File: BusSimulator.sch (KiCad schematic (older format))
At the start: 100 parts, among them IC1 CS30CL, IC2 CS30CL, IC3 CS30CL, J1 CONN_3-6318491-6, J2 OSTTA024163, J3 Conn_01x03, J4 Conn_01x03, J5 Conn_01x02, J6 Conn_01x03, Q1 MOSFET_N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

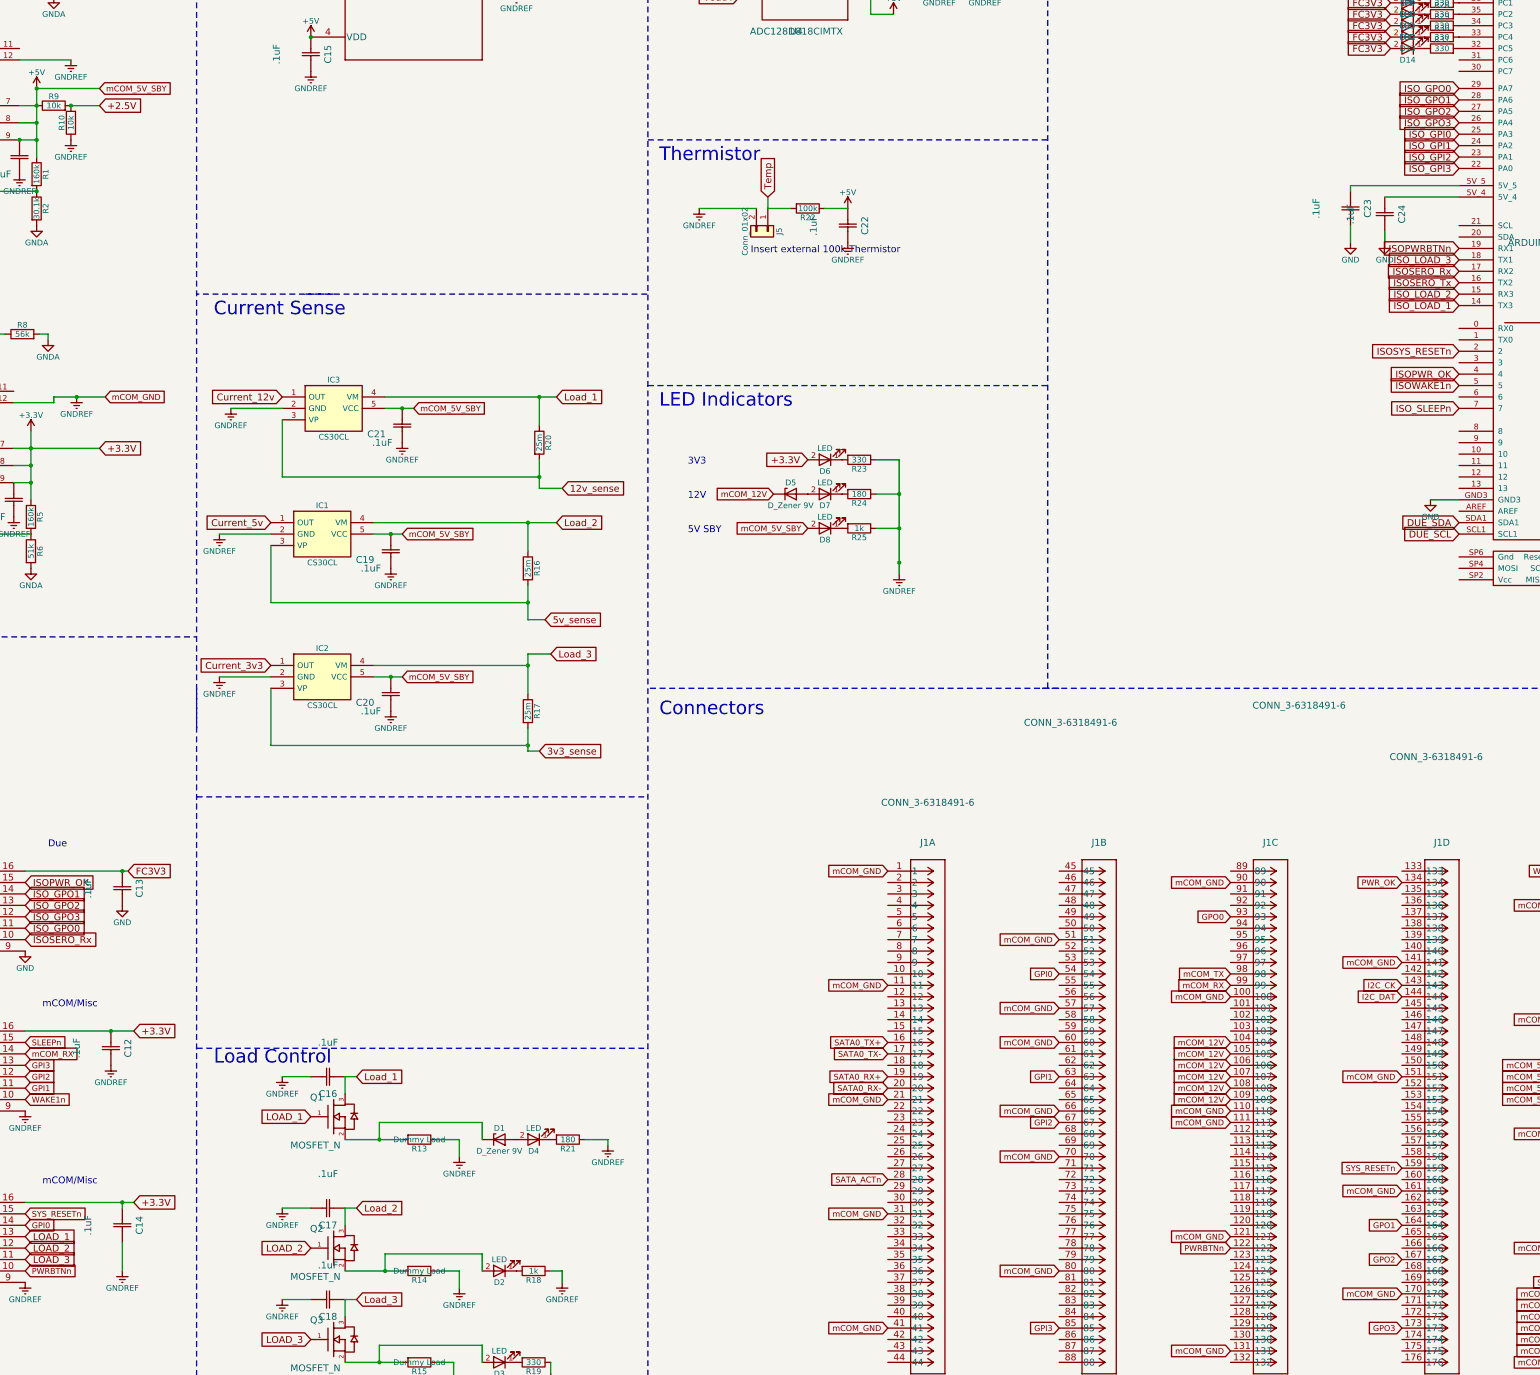
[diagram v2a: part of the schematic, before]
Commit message: Routed mCOM connector and isolators
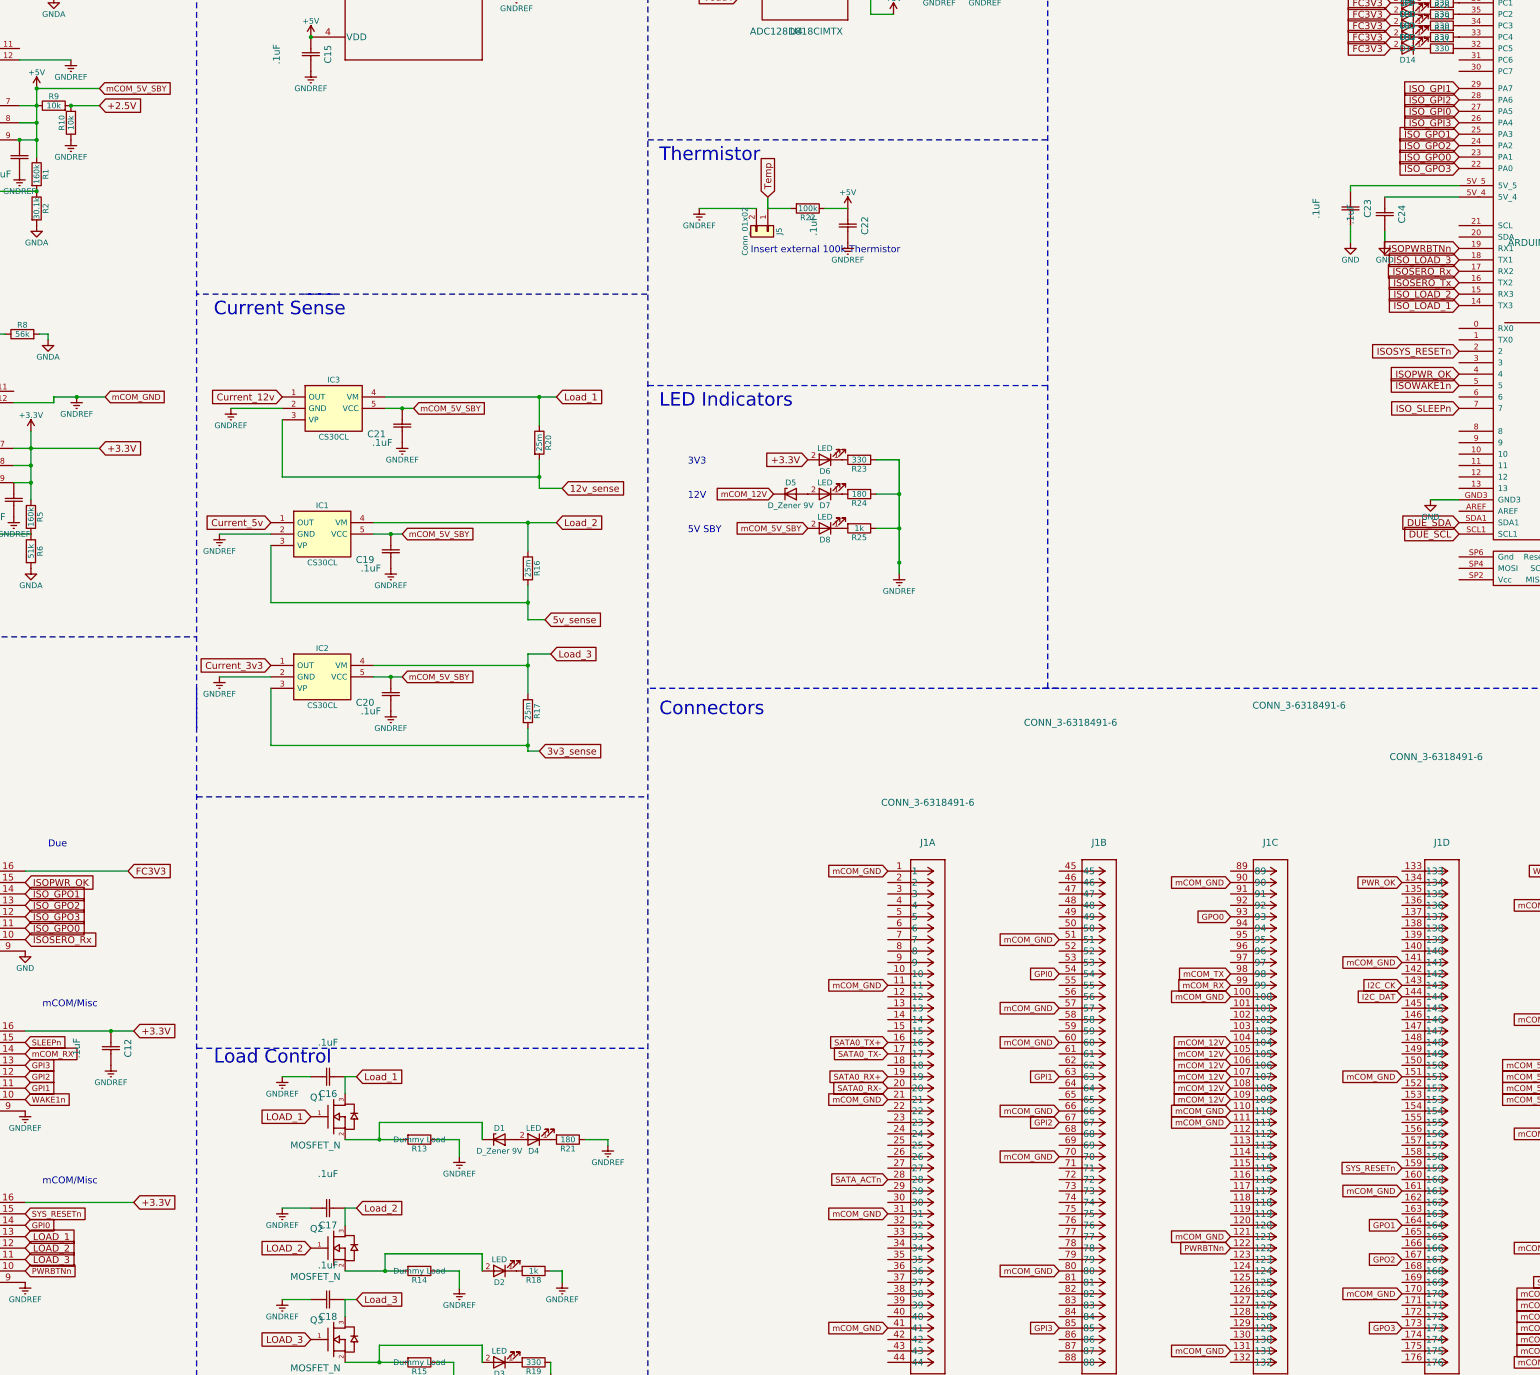
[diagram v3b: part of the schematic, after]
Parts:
- removed C13, C14: .1uF, Capacitors_SMD:C_0603, symbol CAPH
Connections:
- net ISO_GPI0: now also SHIELD1.27 (PA5); no longer SHIELD1.25 (PA3)
- net ISO_GPI1: now also SHIELD1.29 (PA7); no longer SHIELD1.24 (PA2)
- net ISO_GPI2: now also SHIELD1.28 (PA6); no longer SHIELD1.23 (PA1)
- net ISO_GPI3: now also SHIELD1.26 (PA4); no longer SHIELD1.22 (PA0)
- net ISO_GPO0: now also SHIELD1.23 (PA1); no longer SHIELD1.29 (PA7)
- net ISO_GPO1: now also SHIELD1.25 (PA3); no longer SHIELD1.28 (PA6)
- net ISO_GPO2: now also SHIELD1.24 (PA2); no longer SHIELD1.27 (PA5)
- net ISO_GPO3: now also SHIELD1.22 (PA0); no longer SHIELD1.26 (PA4)
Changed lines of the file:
@@
 Text GLabel 16400 5800 0    60   Input ~ 0
 ISO_SLEEPn
-Text GLabel 16400 3400 0    60   Input ~ 0
+Text GLabel 16400 3200 0    60   Input ~ 0
 ISO_GPI0
-Text GLabel 16400 3500 0    60   Input ~ 0
+Text GLabel 16400 3000 0    60   Input ~ 0
 ISO_GPI1
-Text GLabel 16400 3600 0    60   Input ~ 0
+Text GLabel 16400 3100 0    60   Input ~ 0
 ISO_GPI2
-Text GLabel 16400 3700 0    60   Input ~ 0
+Text GLabel 16400 3300 0    60   Input ~ 0
 ISO_GPI3
 Text GLabel 16400 4900 0    60   Input ~ 0
@@
 Text GLabel 16400 5500 0    60   Input ~ 0
 ISOPWR_OK
-Text GLabel 16400 3000 0    60   Input ~ 0
+Text GLabel 16400 3600 0    60   Input ~ 0
 ISO_GPO0
-Text GLabel 16400 3100 0    60   Input ~ 0
+Text GLabel 16400 3400 0    60   Input ~ 0
 ISO_GPO1
-Text GLabel 16400 3200 0    60   Input ~ 0
+Text GLabel 16400 3500 0    60   Input ~ 0
 ISO_GPO2
-Text GLabel 16400 3300 0    60   Input ~ 0
+Text GLabel 16400 3700 0    60   Input ~ 0
 ISO_GPO3
 Text GLabel 16400 4800 0    60   Input ~ 0
@@
 $EndComp
 $Comp
-L CAPH C13
-U 1 1 5A0C9F62
-P 4700 9850
-F 0 "C13" H 4850 10000 60  0000 C CNN
-F 1 ".1uF" H 4850 9550 60  0000 C CNN
-F 2 "Capacitors_SMD:C_0603" H 4850 9490 60  0001 C CNN
-F 3 "" H 4700 9850 60  0000 C CNN
-	1    4700 9850
-	0    1    1    0
-$EndComp
-$Comp
 L CAPH C7
 U 1 1 5A0CA9FF
@@
 $EndComp
 $Comp
-L GND #PWR070
-U 1 1 5A0CB896
-P 4700 10150
-F 0 "#PWR070" H 4700 9900 50  0001 C CNN
-F 1 "GND" H 4700 10000 50  0000 C CNN
-F 2 "" H 4700 10150 50  0001 C CNN
-F 3 "" H 4700 10150 50  0001 C CNN
-	1    4700 10150
-	1    0    0    -1
-$EndComp
-$Comp
 L GND #PWR071
 U 1 1 5A0CBCD4
@@
 $EndComp
 $Comp
-L GNDREF #PWR072
-U 1 1 5A0CBE30
-P 4700 13350
-F 0 "#PWR072" H 4700 13100 50  0001 C CNN
-F 1 "GNDREF" H 4700 13200 50  0000 C CNN
-F 2 "" H 4700 13350 50  0001 C CNN
-F 3 "" H 4700 13350 50  0001 C CNN
-	1    4700 13350
-	1    0    0    -1
-$EndComp
-$Comp
 L CAPH C9
 U 1 1 5A0CBEE8
@@
 F 3 "" H 1250 12450 60  0000 C CNN
 	1    1250 12450
-	0    1    1    0
-$EndComp
-$Comp
-L CAPH C14
-U 1 1 5A0CC466
-P 4700 12800
-F 0 "C14" H 4850 12950 60  0000 C CNN
-F 1 ".1uF" H 4850 12500 60  0000 C CNN
-F 2 "Capacitors_SMD:C_0603" H 4850 12440 60  0001 C CNN
-F 3 "" H 4700 12800 60  0000 C CNN
-	1    4700 12800
 	0    1    1    0
 $EndComp
@@
 Wire Wire Line
 	800  12750 1450 12750
-Connection ~ 4700 9850
 Connection ~ 950  9850
 Connection ~ 1250 12750
@@
 	950  12450 1250 12450
 Wire Wire Line
-	4700 12800 4700 12750
-Connection ~ 4700 12750
-Wire Wire Line
-	4700 13100 4700 13350
-Wire Wire Line
 	1850 14400 1300 14400

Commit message: added leds
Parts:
- removed J3: Conn_01x03, Pin_Headers:Pin_Header_Straight_1x03_Pitch2.54mm, symbol Conn_01x03
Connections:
- net GND: now also J4.3 (Pin_3)
- net GNDREF: no longer J4.3 (Pin_3)
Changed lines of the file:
@@
 $EndComp
 $Comp
-L GND #PWR071
+L GND #PWR070
 U 1 1 5A0CBCD4
 P 950 12450
-F 0 "#PWR071" H 950 12200 50  0001 C CNN
+F 0 "#PWR070" H 950 12200 50  0001 C CNN
 F 1 "GND" H 950 12300 50  0000 C CNN
 F 2 "" H 950 12450 50  0001 C CNN
@@
 $EndComp
 $Comp
-L GNDREF #PWR073
+L GNDREF #PWR071
 U 1 1 5A0CD222
 P 1300 14700
-F 0 "#PWR073" H 1300 14450 50  0001 C CNN
+F 0 "#PWR071" H 1300 14450 50  0001 C CNN
 F 1 "GNDREF" H 1300 14550 50  0000 C CNN
 F 2 "" H 1300 14700 50  0001 C CNN
@@
 $EndComp
 $Comp
-L GND #PWR074
+L GND #PWR072
 U 1 1 5A0CE751
 P 4050 14700
-F 0 "#PWR074" H 4050 14450 50  0001 C CNN
+F 0 "#PWR072" H 4050 14450 50  0001 C CNN
 F 1 "GND" H 4050 14550 50  0000 C CNN
 F 2 "" H 4050 14700 50  0001 C CNN
@@
 $EndComp
 $Comp
-L GNDREF #PWR075
+L GNDREF #PWR073
 U 1 1 5A0CF4E6
 P 4600 11550
-F 0 "#PWR075" H 4600 11300 50  0001 C CNN
+F 0 "#PWR073" H 4600 11300 50  0001 C CNN
 F 1 "GNDREF" H 4600 11400 50  0000 C CNN
 F 2 "" H 4600 11550 50  0001 C CNN
@@
 $EndComp
 $Comp
-L GND #PWR076
+L GND #PWR074
 U 1 1 5A0CF996
 P 700 10950
-F 0 "#PWR076" H 700 10700 50  0001 C CNN
+F 0 "#PWR074" H 700 10700 50  0001 C CNN
 F 1 "GND" H 700 10800 50  0000 C CNN
 F 2 "" H 700 10950 50  0001 C CNN
@@
 $EndComp
 $Comp
-L GNDREF #PWR077
+L GNDREF #PWR075
 U 1 1 5A0D1163
 P 6350 2850
-F 0 "#PWR077" H 6350 2600 50  0001 C CNN
+F 0 "#PWR075" H 6350 2600 50  0001 C CNN
 F 1 "GNDREF" H 6350 2700 50  0000 C CNN
 F 2 "" H 6350 2850 50  0001 C CNN
@@
 $EndComp
 $Comp
-L GNDREF #PWR078
+L GNDREF #PWR076
 U 1 1 5A0D2058
 P 11050 4350
-F 0 "#PWR078" H 11050 4100 50  0001 C CNN
+F 0 "#PWR076" H 11050 4100 50  0001 C CNN
 F 1 "GNDREF" H 11050 4200 50  0000 C CNN
 F 2 "" H 11050 4350 50  0001 C CNN
@@
 $EndComp
 $Comp
-L GND #PWR079
+L GND #PWR077
 U 1 1 5A0D39BB
 P 18800 6500
-F 0 "#PWR079" H 18800 6250 50  0001 C CNN
+F 0 "#PWR077" H 18800 6250 50  0001 C CNN
 F 1 "GND" H 18800 6350 50  0000 C CNN
 F 2 "" H 18800 6500 50  0001 C CNN
@@
 $EndComp
 $Comp
-L GND #PWR080
+L GND #PWR078
 U 1 1 5A0D3A85
 P 19000 5800
-F 0 "#PWR080" H 19000 5550 50  0001 C CNN
+F 0 "#PWR078" H 19000 5550 50  0001 C CNN
 F 1 "GND" H 19000 5650 50  0000 C CNN
 F 2 "" H 19000 5800 50  0001 C CNN
@@
 $EndComp
 $Comp
-L GND #PWR081
+L GND #PWR079
 U 1 1 5A0D45AE
 P 15750 4350
-F 0 "#PWR081" H 15750 4100 50  0001 C CNN
+F 0 "#PWR079" H 15750 4100 50  0001 C CNN
 F 1 "GND" H 15750 4200 50  0000 C CNN
 F 2 "" H 15750 4350 50  0001 C CNN
@@
 $EndComp
 $Comp
-L GND #PWR082
+L GND #PWR080
 U 1 1 5A0D4678
 P 15450 4350
-F 0 "#PWR082" H 15450 4100 50  0001 C CNN
+F 0 "#PWR080" H 15450 4100 50  0001 C CNN
 F 1 "GND" H 15450 4200 50  0000 C CNN
 F 2 "" H 15450 4350 50  0001 C CNN
@@
 $EndComp
 $Comp
-L GNDREF #PWR083
+L GNDREF #PWR081
 U 1 1 5A0DCFAA
 P 18450 10150
-F 0 "#PWR083" H 18450 9900 50  0001 C CNN
+F 0 "#PWR081" H 18450 9900 50  0001 C CNN
 F 1 "GNDREF" H 18450 10000 50  0000 C CNN
 F 2 "" H 18450 10150 50  0001 C CNN
@@
 $EndComp
 $Comp
-L GNDREF #PWR084
+L GNDREF #PWR082
 U 1 1 5A0DD07C
 P 18800 10850
-F 0 "#PWR084" H 18800 10600 50  0001 C CNN
+F 0 "#PWR082" H 18800 10600 50  0001 C CNN
 F 1 "GNDREF" H 18800 10700 50  0000 C CNN
 F 2 "" H 18800 10850 50  0001 C CNN
@@
 $EndComp
 $Comp
-L GNDREF #PWR085
+L GNDREF #PWR083
 U 1 1 5A0DD4EC
 P 22250 11650
-F 0 "#PWR085" H 22250 11400 50  0001 C CNN
+F 0 "#PWR083" H 22250 11400 50  0001 C CNN
 F 1 "GNDREF" H 22250 11500 50  0000 C CNN
 F 2 "" H 22250 11650 50  0001 C CNN
@@
 $EndComp
 $Comp
-L GNDREF #PWR086
+L GNDREF #PWR084
 U 1 1 5A0DDC34
 P 22200 10250
-F 0 "#PWR086" H 22200 10000 50  0001 C CNN
+F 0 "#PWR084" H 22200 10000 50  0001 C CNN
 F 1 "GNDREF" H 22200 10100 50  0000 C CNN
 F 2 "" H 22200 10250 50  0001 C CNN
@@
 $EndComp
 $Comp
-L GNDREF #PWR087
+L GNDREF #PWR085
 U 1 1 5A0DE446
 P 22350 12850
-F 0 "#PWR087" H 22350 12600 50  0001 C CNN
+F 0 "#PWR085" H 22350 12600 50  0001 C CNN
 F 1 "GNDREF" H 22350 12700 50  0000 C CNN
 F 2 "" H 22350 12850 50  0001 C CNN
@@
 $EndComp
 $Comp
-L GNDREF #PWR088
+L GNDREF #PWR086
 U 1 1 5A0E0BE0
 P 6100 12800
-F 0 "#PWR088" H 6100 12550 50  0001 C CNN
+F 0 "#PWR086" H 6100 12550 50  0001 C CNN
 F 1 "GNDREF" H 6100 12650 50  0000 C CNN
 F 2 "" H 6100 12800 50  0001 C CNN
@@
 $EndComp
 $Comp
-L GNDREF #PWR089
+L GNDREF #PWR087
 U 1 1 5A0E0D88
 P 6100 11650
-F 0 "#PWR089" H 6100 11400 50  0001 C CNN
+F 0 "#PWR087" H 6100 11400 50  0001 C CNN
 F 1 "GNDREF" H 6100 11500 50  0000 C CNN
 F 2 "" H 6100 11650 50  0001 C CNN
@@
 $EndComp
 $Comp
-L GNDREF #PWR090
+L GNDREF #PWR088
 U 1 1 5A0E0F30
 P 6100 13600
-F 0 "#PWR090" H 6100 13350 50  0001 C CNN
+F 0 "#PWR088" H 6100 13350 50  0001 C CNN
 F 1 "GNDREF" H 6100 13450 50  0000 C CNN
 F 2 "" H 6100 13600 50  0001 C CNN
@@
 	0    -1   -1   0
 $EndComp
-Text GLabel 2300 15150 0    60   Input ~ 0
-SDASDC
-Text GLabel 2300 15250 0    60   Input ~ 0
-SCLADC
 $Comp
 L Conn_01x03 J6
@@
 $EndComp
 $Comp
-L GNDREF #PWR091
+L GNDREF #PWR089
 U 1 1 5A0B68CF
 P 21700 9200
-F 0 "#PWR091" H 21700 8950 50  0001 C CNN
+F 0 "#PWR089" H 21700 8950 50  0001 C CNN
 F 1 "GNDREF" H 21700 9050 50  0000 C CNN
 F 2 "" H 21700 9200 50  0001 C CNN
@@
 $EndComp
 Wire Wire Line
-	2250 15350 2300 15350
-$Comp
-L GNDREF #PWR092
-U 1 1 5A0B4819
-P 2250 15350
-F 0 "#PWR092" H 2250 15100 50  0001 C CNN
-F 1 "GNDREF" H 2250 15200 50  0000 C CNN
-F 2 "" H 2250 15350 50  0001 C CNN
-F 3 "" H 2250 15350 50  0001 C CNN
-	1    2250 15350
-	1    0    0    -1
-$EndComp
-$Comp
-L Conn_01x03 J3
-U 1 1 5A0B44FF
-P 2500 15250
-F 0 "J3" H 2500 15450 50  0000 C CNN
-F 1 "Conn_01x03" H 2500 15050 50  0000 C CNN
-F 2 "Pin_Headers:Pin_Header_Straight_1x03_Pitch2.54mm" H 2500 15250 50  0001 C CNN
-F 3 "" H 2500 15250 50  0001 C CNN
-	1    2500 15250
-	1    0    0    -1
-$EndComp
-Wire Wire Line
 	3450 15350 3500 15350
-$Comp
-L GNDREF #PWR093
-U 1 1 5A0B8740
-P 3450 15350
-F 0 "#PWR093" H 3450 15100 50  0001 C CNN
-F 1 "GNDREF" H 3450 15200 50  0000 C CNN
-F 2 "" H 3450 15350 50  0001 C CNN
-F 3 "" H 3450 15350 50  0001 C CNN
-	1    3450 15350
-	1    0    0    -1
-$EndComp
 $Comp
 L Conn_01x03 J4
@@
 Text GLabel 6350 13950 0    60   Input ~ 0
 LOAD_3
+$Comp
+L GND #PWR091
+U 1 1 5A0A7E15
+P 3450 15350
+F 0 "#PWR091" H 3450 15100 50  0001 C CNN
+F 1 "GND" H 3450 15200 50  0000 C CNN
+F 2 "" H 3450 15350 50  0001 C CNN
+F 3 "" H 3450 15350 50  0001 C CNN
+	1    3450 15350
+	1    0    0    -1
+$EndComp
+Text GLabel 4500 900  2    60   Input ~ 0
+mCom_12V
+Wire Wire Line
+	4500 900  4350 900
+Wire Wire Line
+	4350 900  4350 1000
+Connection ~ 4350 1000
 $EndSCHEMATC

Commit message: zoning fix
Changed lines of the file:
@@
 LOAD_3
 $Comp
-L GND #PWR091
+L GND #PWR090
 U 1 1 5A0A7E15
 P 3450 15350
-F 0 "#PWR091" H 3450 15100 50  0001 C CNN
+F 0 "#PWR090" H 3450 15100 50  0001 C CNN
 F 1 "GND" H 3450 15200 50  0000 C CNN
 F 2 "" H 3450 15350 50  0001 C CNN
@@
 	4350 900  4350 1000
 Connection ~ 4350 1000
+Text GLabel 4400 3450 2    60   Input ~ 0
+mCOM_GND
+Wire Wire Line
+	4250 3450 4400 3450
 $EndSCHEMATC
